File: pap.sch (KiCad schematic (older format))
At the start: 0 parts

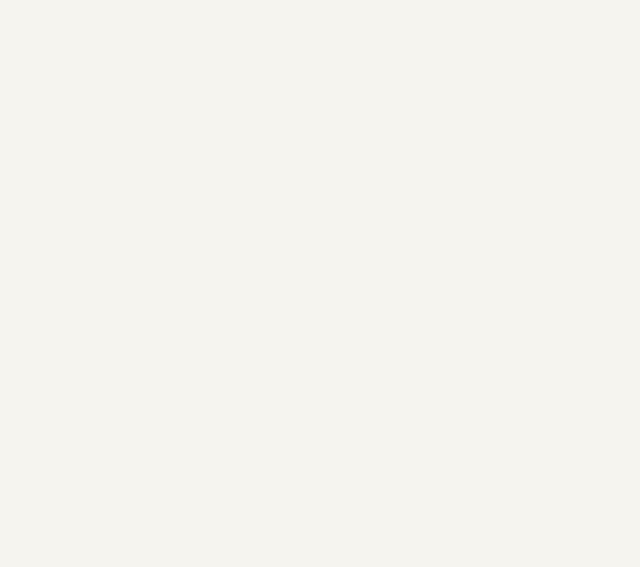
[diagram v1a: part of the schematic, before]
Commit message: termino ruteo, genero gerbers y drills, y entrego
Listo pisto, lo dejo asi, ya lo revise varias veces, agregue los
desacoples y el bulk pendiente, coloreo leds con nuevo 3d, genero
gerners, y agrego valores a los componentes. ha y tambien dejo PTH los
agujeros de los tornillos, quedan mejor. y no mucho mas.. entrego ya!
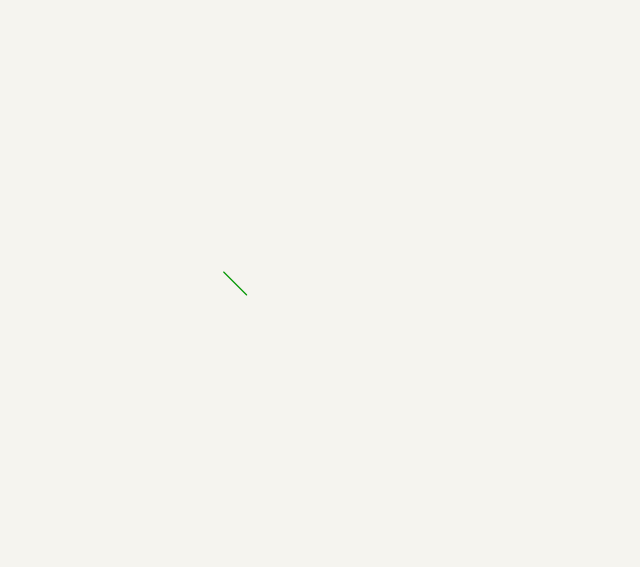
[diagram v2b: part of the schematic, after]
